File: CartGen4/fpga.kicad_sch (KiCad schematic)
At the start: 1 part

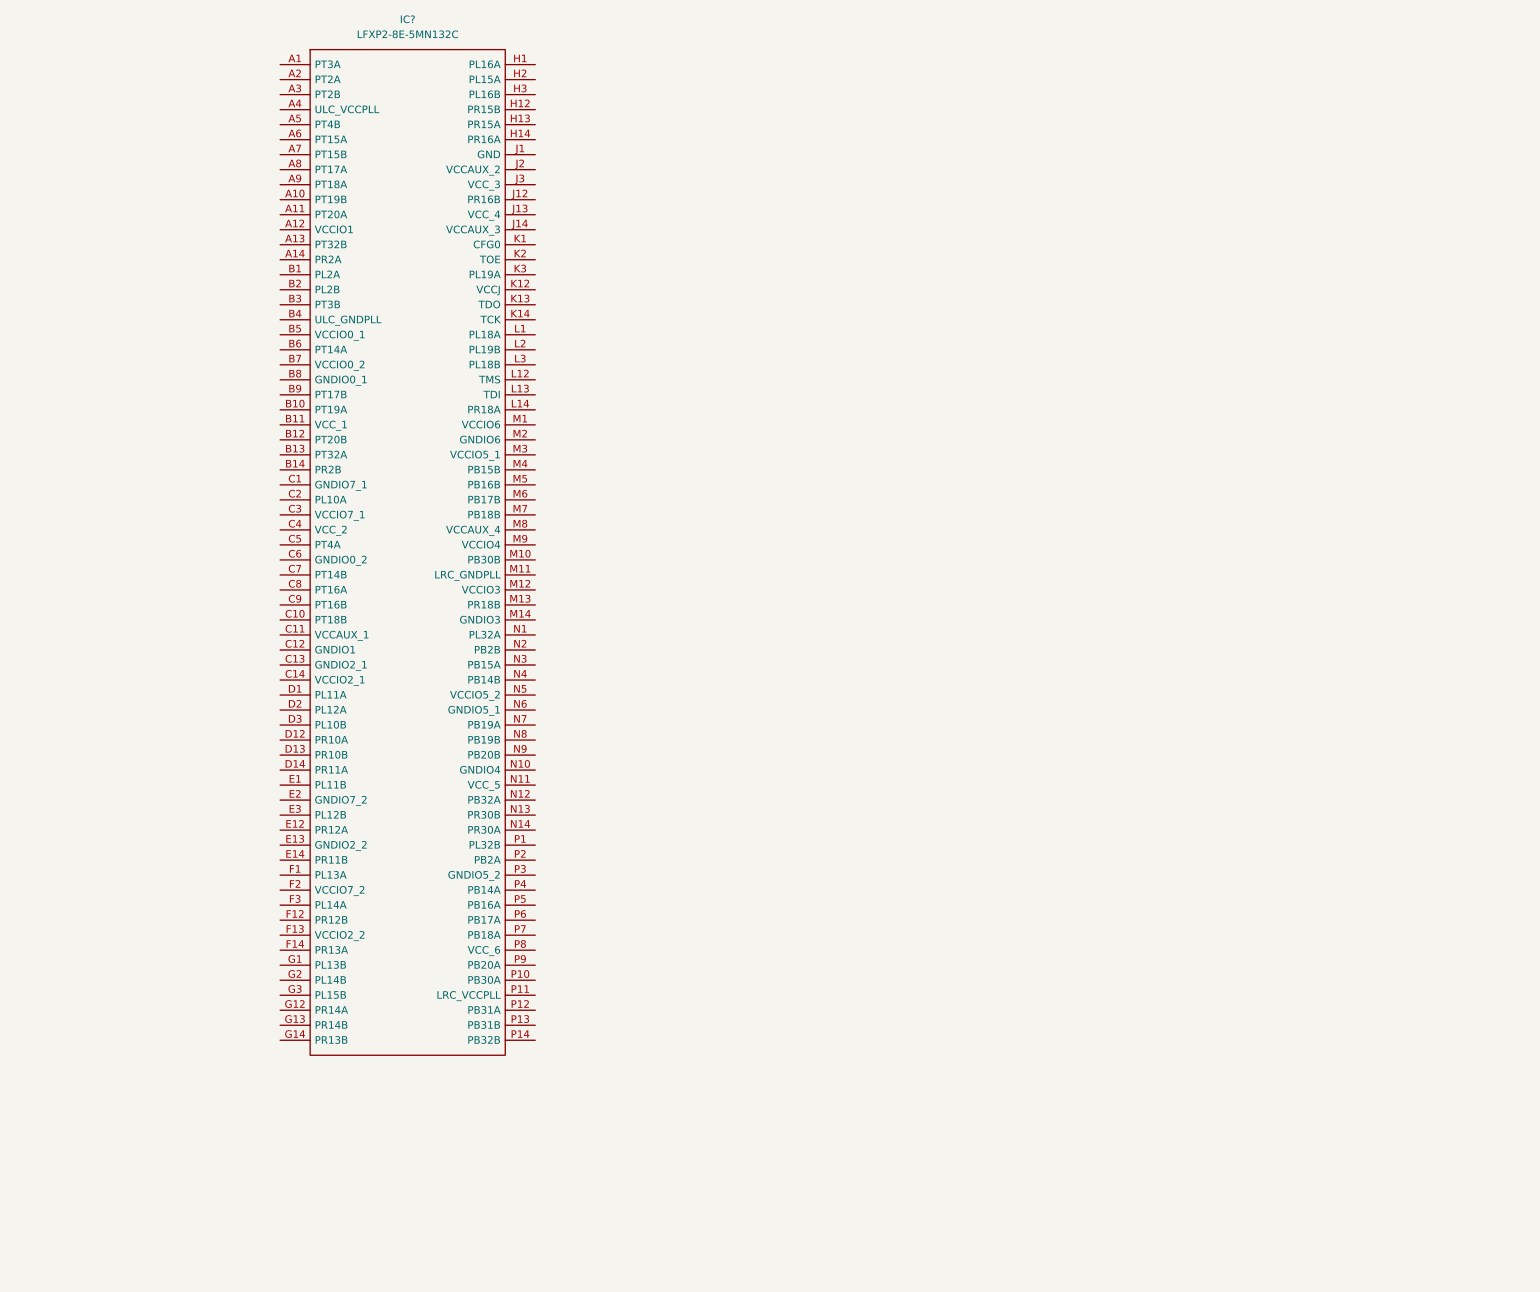
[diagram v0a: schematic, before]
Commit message: Added FPGA and RAM symbols
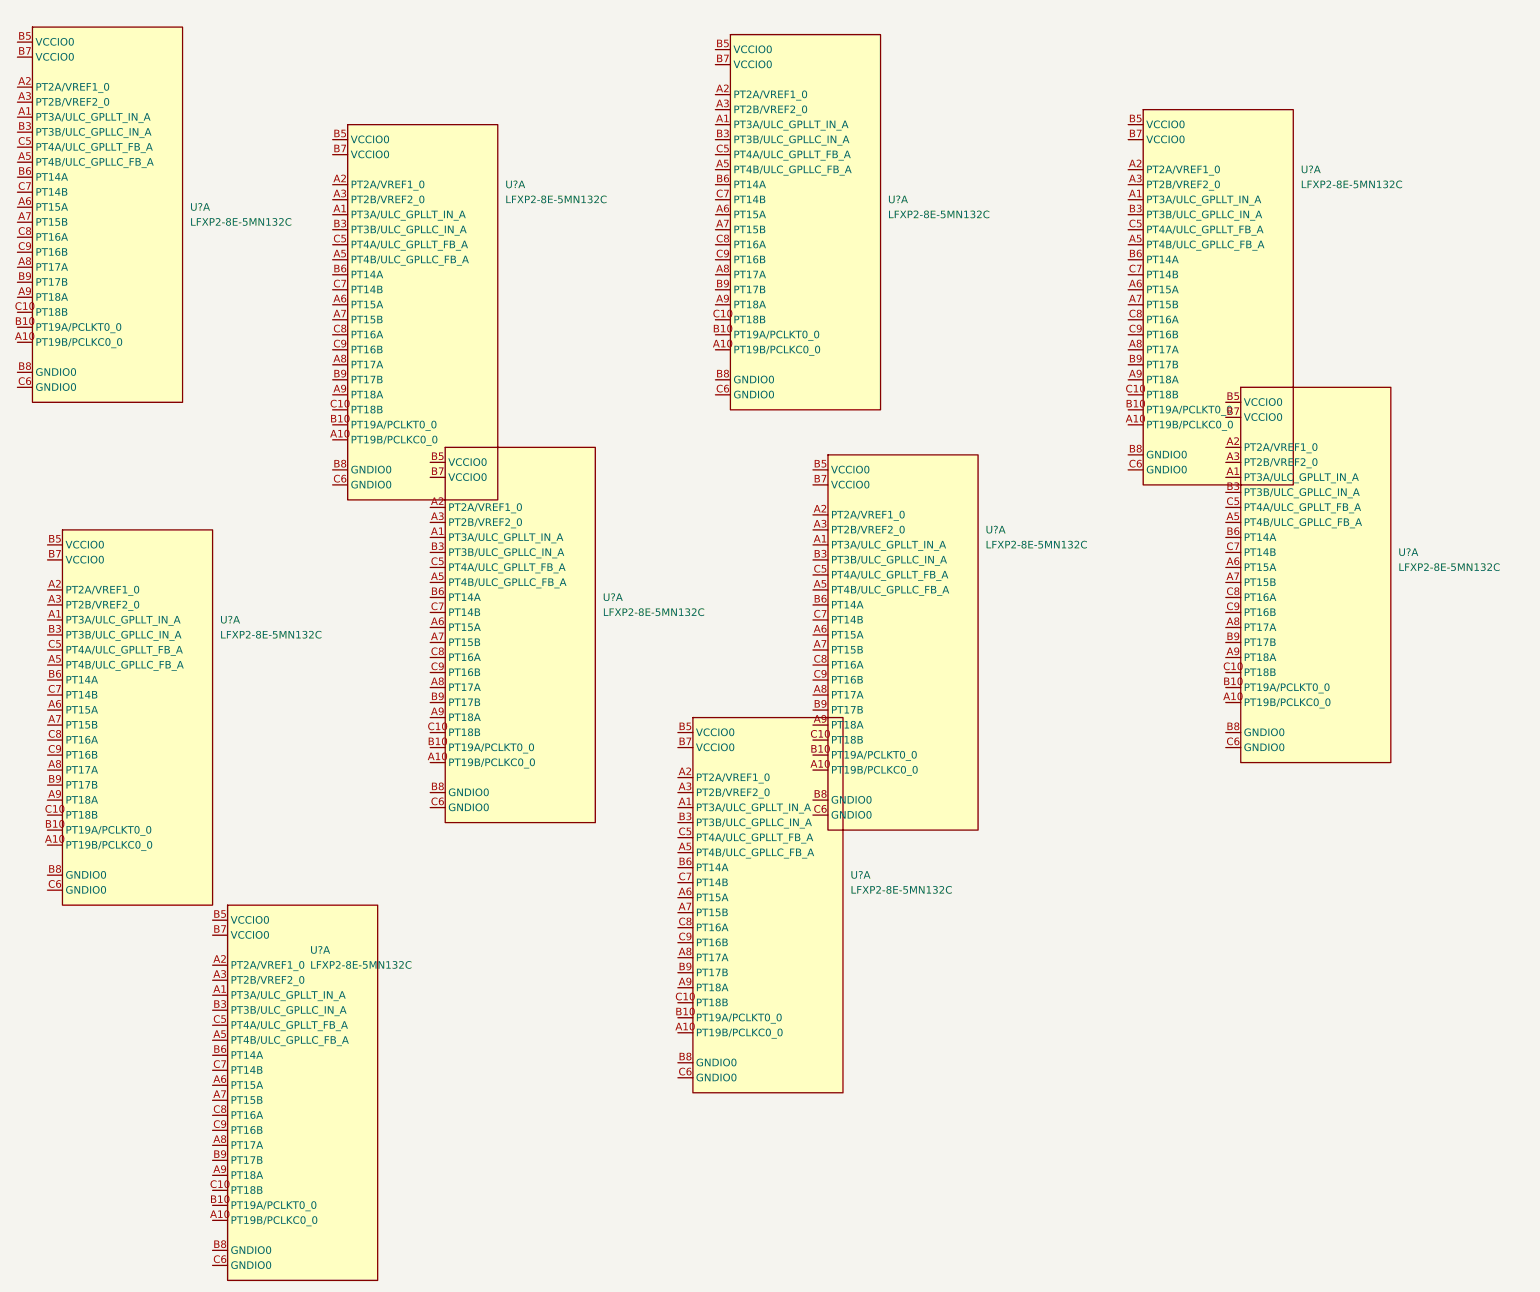
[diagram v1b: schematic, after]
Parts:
- removed IC?: LFXP2-8E-5MN132C, BGA132C50P14X14_800X800X135, symbol SamacSys_Parts:LFXP2-8E-5MN132C
- added U? (x10): LFXP2-8E-5MN132C, symbol FPGA_Lattice:LFXP2-8E-5MN132C

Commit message: Added RAM and clock
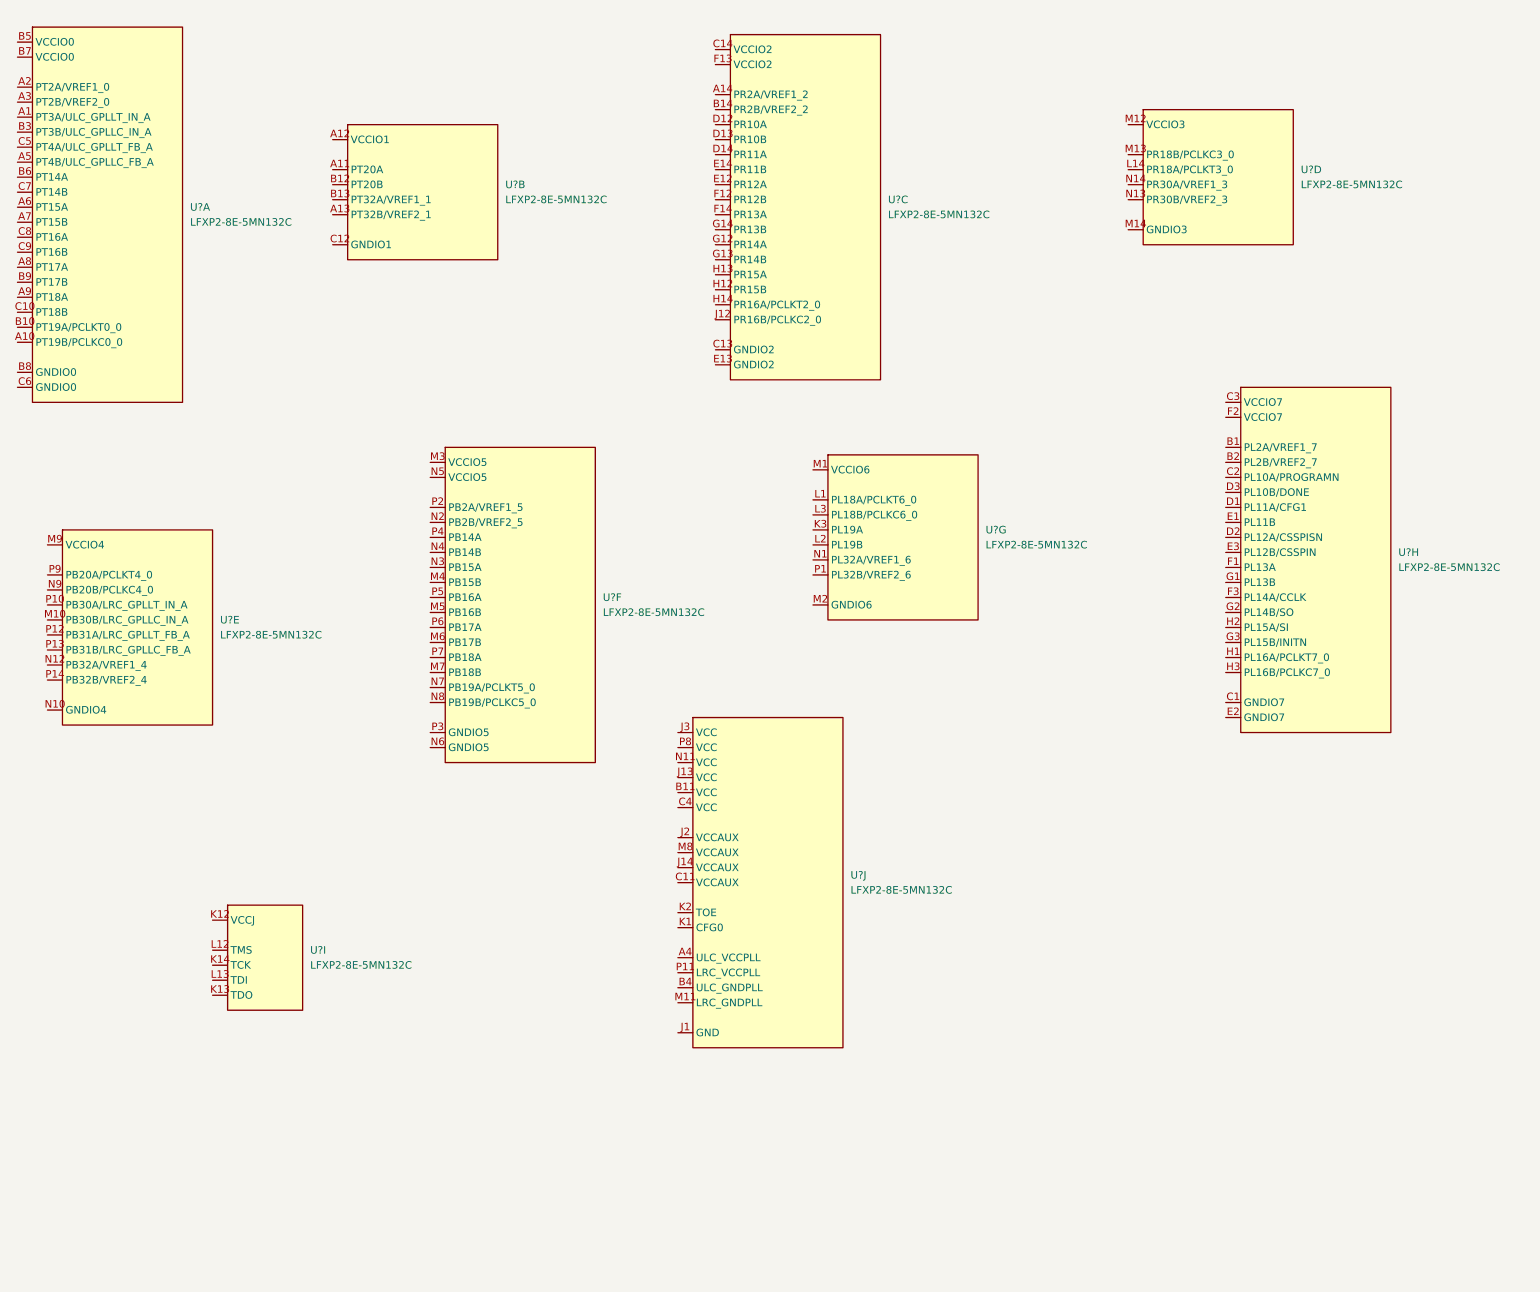
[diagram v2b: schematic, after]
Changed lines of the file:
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@@
     (title "FPGA")
   )
-  (symbol (lib_id "FPGA_Lattice:LFXP2-8E-5MN132C") (at 35.56 104.14 0)
+  (symbol (lib_id "FPGA_Lattice:LFXP2-8E-5MN132C") (at 35.56 104.14 0) (unit 5)
     (in_bom yes) (on_board yes) (fields_autoplaced)
     (property "Reference" "U?" (id 0) (at 62.23 119.3799 0)
@@
     (pin "P9")
   )
-  (symbol (lib_id "FPGA_Lattice:LFXP2-8E-5MN132C") (at 83.82 35.56 0)
+  (symbol (lib_id "FPGA_Lattice:LFXP2-8E-5MN132C") (at 83.82 35.56 0) (unit 2)
     (in_bom yes) (on_board yes) (fields_autoplaced)
     (property "Reference" "U?" (id 0) (at 110.49 45.7199 0)
@@
     (pin "C12")
   )
-  (symbol (lib_id "FPGA_Lattice:LFXP2-8E-5MN132C") (at 142.24 135.89 0)
+  (symbol (lib_id "FPGA_Lattice:LFXP2-8E-5MN132C") (at 142.24 135.89 0) (unit 10)
     (in_bom yes) (on_board yes) (fields_autoplaced)
     (property "Reference" "U?" (id 0) (at 168.91 162.5599 0)
@@
     (pin "P8")
   )
-  (symbol (lib_id "FPGA_Lattice:LFXP2-8E-5MN132C") (at 234.95 80.01 0)
+  (symbol (lib_id "FPGA_Lattice:LFXP2-8E-5MN132C") (at 234.95 80.01 0) (unit 8)
     (in_bom yes) (on_board yes) (fields_autoplaced)
     (property "Reference" "U?" (id 0) (at 261.62 107.9499 0)
@@
     (pin "H3")
   )
-  (symbol (lib_id "FPGA_Lattice:LFXP2-8E-5MN132C") (at 30.48 19.05 0)
+  (symbol (lib_id "FPGA_Lattice:LFXP2-8E-5MN132C") (at 30.48 19.05 0) (unit 1)
     (in_bom yes) (on_board yes) (fields_autoplaced)
     (property "Reference" "U?" (id 0) (at 57.15 49.5299 0)
@@
     (pin "C9")
   )
-  (symbol (lib_id "FPGA_Lattice:LFXP2-8E-5MN132C") (at 63.5 167.64 0)
+  (symbol (lib_id "FPGA_Lattice:LFXP2-8E-5MN132C") (at 63.5 167.64 0) (unit 9)
     (in_bom yes) (on_board yes) (fields_autoplaced)
     (property "Reference" "U?" (id 0) (at 77.47 175.2599 0)
@@
     (pin "L13")
   )
-  (symbol (lib_id "FPGA_Lattice:LFXP2-8E-5MN132C") (at 100.33 90.17 0)
+  (symbol (lib_id "FPGA_Lattice:LFXP2-8E-5MN132C") (at 100.33 90.17 0) (unit 6)
     (in_bom yes) (on_board yes) (fields_autoplaced)
     (property "Reference" "U?" (id 0) (at 127 115.5699 0)
@@
     (pin "P7")
   )
-  (symbol (lib_id "FPGA_Lattice:LFXP2-8E-5MN132C") (at 218.44 33.02 0)
+  (symbol (lib_id "FPGA_Lattice:LFXP2-8E-5MN132C") (at 218.44 33.02 0) (unit 4)
     (in_bom yes) (on_board yes) (fields_autoplaced)
     (property "Reference" "U?" (id 0) (at 245.11 43.1799 0)
@@
     (pin "N14")
   )
-  (symbol (lib_id "FPGA_Lattice:LFXP2-8E-5MN132C") (at 165.1 91.44 0)
+  (symbol (lib_id "FPGA_Lattice:LFXP2-8E-5MN132C") (at 165.1 91.44 0) (unit 7)
     (in_bom yes) (on_board yes) (fields_autoplaced)
     (property "Reference" "U?" (id 0) (at 191.77 104.1399 0)
@@
     (pin "P1")
   )
-  (symbol (lib_id "FPGA_Lattice:LFXP2-8E-5MN132C") (at 148.59 20.32 0)
+  (symbol (lib_id "FPGA_Lattice:LFXP2-8E-5MN132C") (at 148.59 20.32 0) (unit 3)
     (in_bom yes) (on_board yes) (fields_autoplaced)
     (property "Reference" "U?" (id 0) (at 175.26 48.2599 0)
